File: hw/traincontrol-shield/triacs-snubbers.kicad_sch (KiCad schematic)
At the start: 6 parts, among them Q1 BT134W-600D, Q2 BT134W-600D

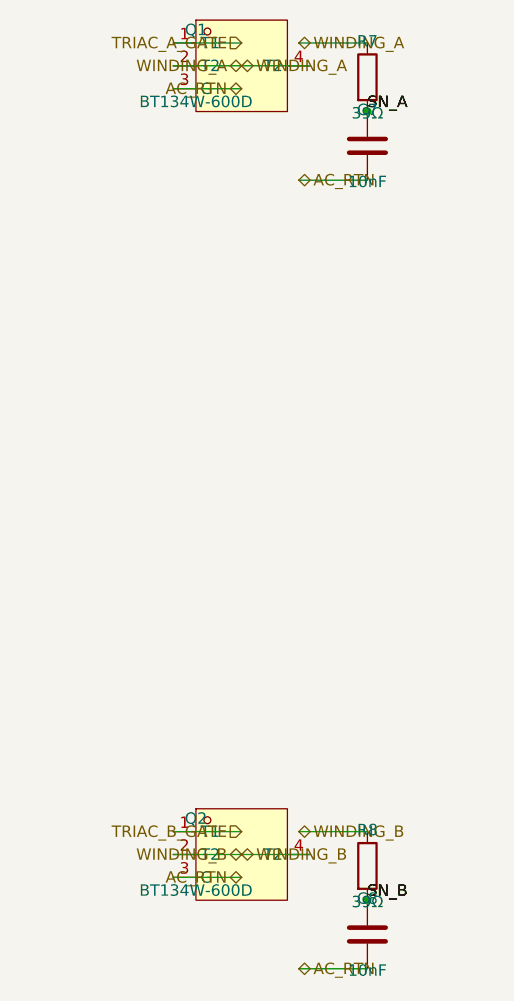
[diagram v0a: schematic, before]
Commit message: Fix hierarchical label placement and orientation in sub-sheets
Root cause: hlabel() placed the label at lx (stub tip) instead of x
(circuit connection point), mirroring the Issue-2 glabel bug fixed in
commit 2270223.

Fix applied to hlabel():
  (at {lx} ...) → (at {x} ...)  — label now sits at the circuit endpoint

Angle convention (matches label body direction):
  angle=180 → body extends LEFT  — left-side input/bidirectional labels
  angle=0   → body extends RIGHT — right-side output/bidirectional labels

Sheets affected: zero-crossing, xor-interlock, opto-triac-drive,
rail-voltage-sense; triacs-snubbers and mcu already had correct angles.

Co-Authored-By: Claude Sonnet 4.6 <noreply@anthropic.com>
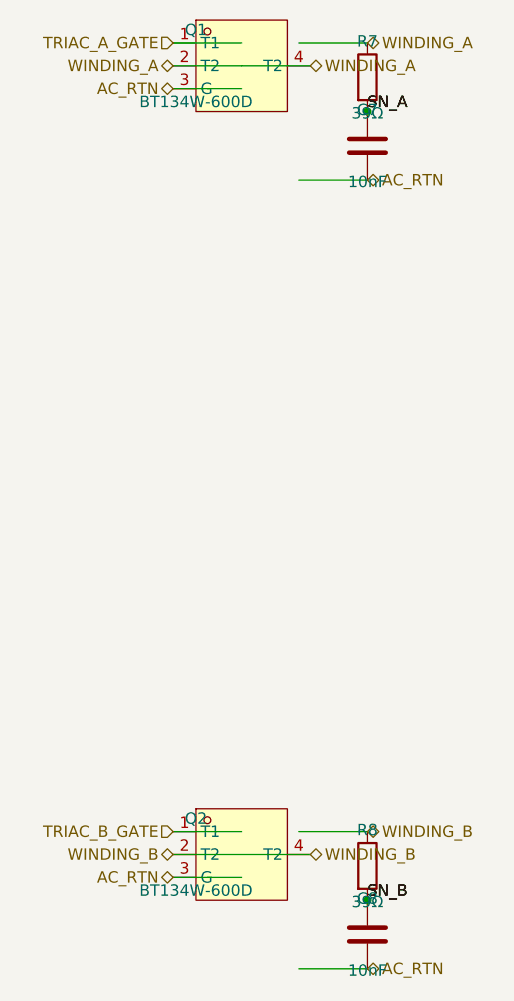
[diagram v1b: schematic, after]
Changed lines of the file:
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@@
 	(hierarchical_label "AC_RTN"
 		(shape bidirectional)
-		(at 85.09 92.71000000000001 180)
-		(fields_autoplaced yes)
-		(effects (font (size 1.27 1.27)) (justify right bottom))
-		(property "Intersheetrefs" "${INTERSHEET_REFS}"
-			(at 85.09 92.71000000000001 0)
+		(at 77.47 92.71000000000001 180)
+		(fields_autoplaced yes)
+		(effects (font (size 1.27 1.27)) (justify right bottom))
+		(property "Intersheetrefs" "${INTERSHEET_REFS}"
+			(at 77.47 92.71000000000001 0)
 			(effects (font (size 1.27 1.27)) (hide yes))
 		)
@@
 	(hierarchical_label "WINDING_A"
 		(shape bidirectional)
-		(at 85.09 90.17 180)
-		(fields_autoplaced yes)
-		(effects (font (size 1.27 1.27)) (justify right bottom))
-		(property "Intersheetrefs" "${INTERSHEET_REFS}"
-			(at 85.09 90.17 0)
+		(at 77.47 90.17 180)
+		(fields_autoplaced yes)
+		(effects (font (size 1.27 1.27)) (justify right bottom))
+		(property "Intersheetrefs" "${INTERSHEET_REFS}"
+			(at 77.47 90.17 0)
 			(effects (font (size 1.27 1.27)) (hide yes))
 		)
@@
 	(hierarchical_label "WINDING_A"
 		(shape bidirectional)
-		(at 85.09 90.17 0)
-		(fields_autoplaced yes)
-		(effects (font (size 1.27 1.27)) (justify left bottom))
-		(property "Intersheetrefs" "${INTERSHEET_REFS}"
-			(at 85.09 90.17 0)
+		(at 92.71000000000001 90.17 0)
+		(fields_autoplaced yes)
+		(effects (font (size 1.27 1.27)) (justify left bottom))
+		(property "Intersheetrefs" "${INTERSHEET_REFS}"
+			(at 92.71000000000001 90.17 0)
 			(effects (font (size 1.27 1.27)) (hide yes))
 		)
@@
 	(hierarchical_label "TRIAC_A_GATE"
 		(shape input)
-		(at 85.09 87.63 180)
-		(fields_autoplaced yes)
-		(effects (font (size 1.27 1.27)) (justify right bottom))
-		(property "Intersheetrefs" "${INTERSHEET_REFS}"
-			(at 85.09 87.63 0)
+		(at 77.47 87.63 180)
+		(fields_autoplaced yes)
+		(effects (font (size 1.27 1.27)) (justify right bottom))
+		(property "Intersheetrefs" "${INTERSHEET_REFS}"
+			(at 77.47 87.63 0)
 			(effects (font (size 1.27 1.27)) (hide yes))
 		)
@@
 	(hierarchical_label "WINDING_A"
 		(shape bidirectional)
-		(at 91.44 87.63 0)
-		(fields_autoplaced yes)
-		(effects (font (size 1.27 1.27)) (justify left bottom))
-		(property "Intersheetrefs" "${INTERSHEET_REFS}"
-			(at 91.44 87.63 0)
+		(at 99.06 87.63 0)
+		(fields_autoplaced yes)
+		(effects (font (size 1.27 1.27)) (justify left bottom))
+		(property "Intersheetrefs" "${INTERSHEET_REFS}"
+			(at 99.06 87.63 0)
 			(effects (font (size 1.27 1.27)) (hide yes))
 		)
@@
 	(hierarchical_label "AC_RTN"
 		(shape bidirectional)
-		(at 91.44 102.87 0)
-		(fields_autoplaced yes)
-		(effects (font (size 1.27 1.27)) (justify left bottom))
-		(property "Intersheetrefs" "${INTERSHEET_REFS}"
-			(at 91.44 102.87 0)
+		(at 99.06 102.87 0)
+		(fields_autoplaced yes)
+		(effects (font (size 1.27 1.27)) (justify left bottom))
+		(property "Intersheetrefs" "${INTERSHEET_REFS}"
+			(at 99.06 102.87 0)
 			(effects (font (size 1.27 1.27)) (hide yes))
 		)
@@
 	(hierarchical_label "AC_RTN"
 		(shape bidirectional)
-		(at 85.09 180.34 180)
-		(fields_autoplaced yes)
-		(effects (font (size 1.27 1.27)) (justify right bottom))
-		(property "Intersheetrefs" "${INTERSHEET_REFS}"
-			(at 85.09 180.34 0)
+		(at 77.47 180.34 180)
+		(fields_autoplaced yes)
+		(effects (font (size 1.27 1.27)) (justify right bottom))
+		(property "Intersheetrefs" "${INTERSHEET_REFS}"
+			(at 77.47 180.34 0)
 			(effects (font (size 1.27 1.27)) (hide yes))
 		)
@@
 	(hierarchical_label "WINDING_B"
 		(shape bidirectional)
-		(at 85.09 177.8 180)
-		(fields_autoplaced yes)
-		(effects (font (size 1.27 1.27)) (justify right bottom))
-		(property "Intersheetrefs" "${INTERSHEET_REFS}"
-			(at 85.09 177.8 0)
+		(at 77.47 177.8 180)
+		(fields_autoplaced yes)
+		(effects (font (size 1.27 1.27)) (justify right bottom))
+		(property "Intersheetrefs" "${INTERSHEET_REFS}"
+			(at 77.47 177.8 0)
 			(effects (font (size 1.27 1.27)) (hide yes))
 		)
@@
 	(hierarchical_label "WINDING_B"
 		(shape bidirectional)
-		(at 85.09 177.8 0)
-		(fields_autoplaced yes)
-		(effects (font (size 1.27 1.27)) (justify left bottom))
-		(property "Intersheetrefs" "${INTERSHEET_REFS}"
-			(at 85.09 177.8 0)
+		(at 92.71000000000001 177.8 0)
+		(fields_autoplaced yes)
+		(effects (font (size 1.27 1.27)) (justify left bottom))
+		(property "Intersheetrefs" "${INTERSHEET_REFS}"
+			(at 92.71000000000001 177.8 0)
 			(effects (font (size 1.27 1.27)) (hide yes))
 		)
@@
 	(hierarchical_label "TRIAC_B_GATE"
 		(shape input)
-		(at 85.09 175.26000000000002 180)
-		(fields_autoplaced yes)
-		(effects (font (size 1.27 1.27)) (justify right bottom))
-		(property "Intersheetrefs" "${INTERSHEET_REFS}"
-			(at 85.09 175.26000000000002 0)
+		(at 77.47 175.26000000000002 180)
+		(fields_autoplaced yes)
+		(effects (font (size 1.27 1.27)) (justify right bottom))
+		(property "Intersheetrefs" "${INTERSHEET_REFS}"
+			(at 77.47 175.26000000000002 0)
 			(effects (font (size 1.27 1.27)) (hide yes))
 		)
@@
 	(hierarchical_label "WINDING_B"
 		(shape bidirectional)
-		(at 91.44 175.26000000000002 0)
-		(fields_autoplaced yes)
-		(effects (font (size 1.27 1.27)) (justify left bottom))
-		(property "Intersheetrefs" "${INTERSHEET_REFS}"
-			(at 91.44 175.26000000000002 0)
+		(at 99.06 175.26000000000002 0)
+		(fields_autoplaced yes)
+		(effects (font (size 1.27 1.27)) (justify left bottom))
+		(property "Intersheetrefs" "${INTERSHEET_REFS}"
+			(at 99.06 175.26000000000002 0)
 			(effects (font (size 1.27 1.27)) (hide yes))
 		)
@@
 	(hierarchical_label "AC_RTN"
 		(shape bidirectional)
-		(at 91.44 190.50000000000003 0)
-		(fields_autoplaced yes)
-		(effects (font (size 1.27 1.27)) (justify left bottom))
-		(property "Intersheetrefs" "${INTERSHEET_REFS}"
-			(at 91.44 190.50000000000003 0)
-			(effects (font (size 1.27 1.27)) (hide yes))
-		)
+		(at 99.06 190.50000000000003 0)
+		(fields_autoplaced yes)
+		(effects (font (size 1.27 1.27)) (justify left bottom))
+		(property "Intersheetrefs" "${INTERSHEET_REFS}"
+			(at 99.06 190.50000000000003 0)
+			(effects (font (size 1.27 1.27)) (hide yes))
+		)

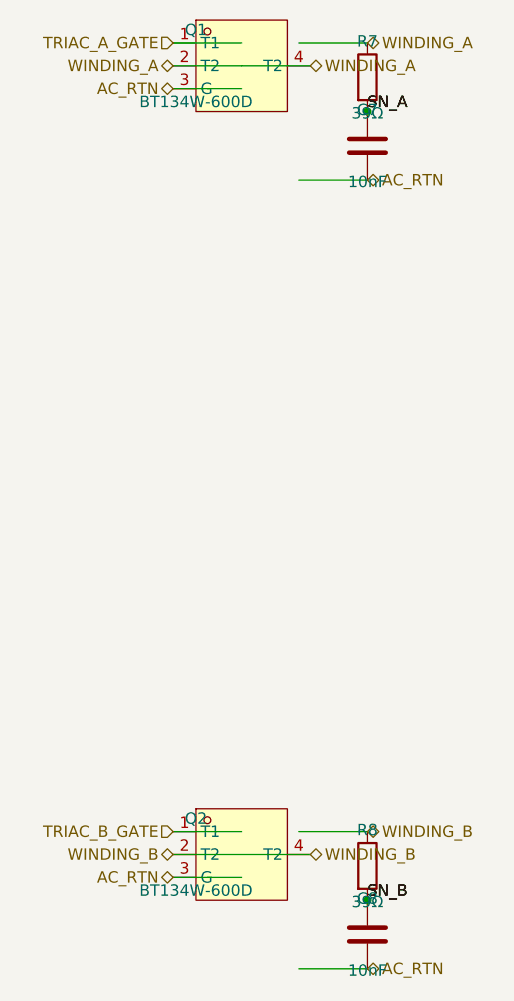
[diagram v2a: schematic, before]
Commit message: Fix hlabel stub direction: stubs now extend away from IC, not into it
Root cause: hlabel() used dx = +STUB for angle=180 and -STUB for angle=0,
which caused every stub wire to run INTO the IC body instead of outward.
This made wires appear to connect at the inner (wrong) end of all pins.

Fix: negate dx so stubs always extend outward from the pin tip:
  angle=180 (left-side input):  dx = -STUB → stub extends LEFT  ✓
  angle=0   (right-side output): dx = +STUB → stub extends RIGHT ✓

Also revert the x-position workarounds that compensated for the wrong
stub direction (zero-crossing AC_IN, opto-triac PHASE/GATE, power-supply
AC_IN/RTN): these are now back at the actual component pin positions.

All 8 sheets validate with kicad-cli.

Co-Authored-By: Claude Sonnet 4.6 <noreply@anthropic.com>
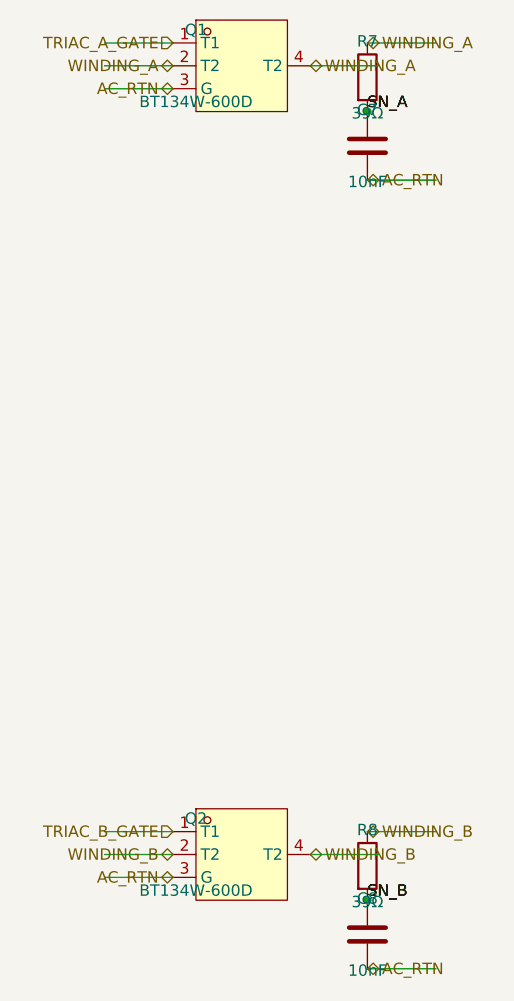
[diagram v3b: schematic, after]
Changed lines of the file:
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@@
 	)
 	(wire
-		(pts (xy 77.47 92.71000000000001) (xy 85.09 92.71000000000001))
+		(pts (xy 69.85 92.71000000000001) (xy 77.47 92.71000000000001))
 		(stroke (width 0) (type solid))
 	)
@@
 	)
 	(wire
-		(pts (xy 77.47 90.17) (xy 85.09 90.17))
+		(pts (xy 69.85 90.17) (xy 77.47 90.17))
 		(stroke (width 0) (type solid))
 	)
@@
 	)
 	(wire
-		(pts (xy 85.09 90.17) (xy 92.71000000000001 90.17))
+		(pts (xy 92.71000000000001 90.17) (xy 100.33000000000001 90.17))
 		(stroke (width 0) (type solid))
 	)
@@
 	)
 	(wire
-		(pts (xy 77.47 87.63) (xy 85.09 87.63))
+		(pts (xy 69.85 87.63) (xy 77.47 87.63))
 		(stroke (width 0) (type solid))
 	)
@@
 	)
 	(wire
-		(pts (xy 91.44 87.63) (xy 99.06 87.63))
+		(pts (xy 99.06 87.63) (xy 106.68 87.63))
 		(stroke (width 0) (type solid))
 	)
@@
 	)
 	(wire
-		(pts (xy 91.44 102.87) (xy 99.06 102.87))
+		(pts (xy 99.06 102.87) (xy 106.68 102.87))
 		(stroke (width 0) (type solid))
 	)
@@
 	)
 	(wire
-		(pts (xy 77.47 180.34) (xy 85.09 180.34))
+		(pts (xy 69.85 180.34) (xy 77.47 180.34))
 		(stroke (width 0) (type solid))
 	)
@@
 	)
 	(wire
-		(pts (xy 77.47 177.8) (xy 85.09 177.8))
+		(pts (xy 69.85 177.8) (xy 77.47 177.8))
 		(stroke (width 0) (type solid))
 	)
@@
 	)
 	(wire
-		(pts (xy 85.09 177.8) (xy 92.71000000000001 177.8))
+		(pts (xy 92.71000000000001 177.8) (xy 100.33000000000001 177.8))
 		(stroke (width 0) (type solid))
 	)
@@
 	)
 	(wire
-		(pts (xy 77.47 175.26000000000002) (xy 85.09 175.26000000000002))
+		(pts (xy 69.85 175.26000000000002) (xy 77.47 175.26000000000002))
 		(stroke (width 0) (type solid))
 	)
@@
 	)
 	(wire
-		(pts (xy 91.44 175.26000000000002) (xy 99.06 175.26000000000002))
+		(pts (xy 99.06 175.26000000000002) (xy 106.68 175.26000000000002))
 		(stroke (width 0) (type solid))
 	)
@@
 	)
 	(wire
-		(pts (xy 91.44 190.50000000000003) (xy 99.06 190.50000000000003))
-		(stroke (width 0) (type solid))
-	)
+		(pts (xy 99.06 190.50000000000003) (xy 106.68 190.50000000000003))
+		(stroke (width 0) (type solid))
+	)
